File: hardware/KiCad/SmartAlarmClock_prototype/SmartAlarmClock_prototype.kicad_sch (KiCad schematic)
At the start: 18 parts, among them J1 YD-ESP32-S3 dev board, J2 MAX7219 32x8 module, J3 DS3231 RTC module (ZS-042), J4 Touch electrode, Q1 BSS138, Q2 BSS138, Q3 BSS138, Q4 BS170

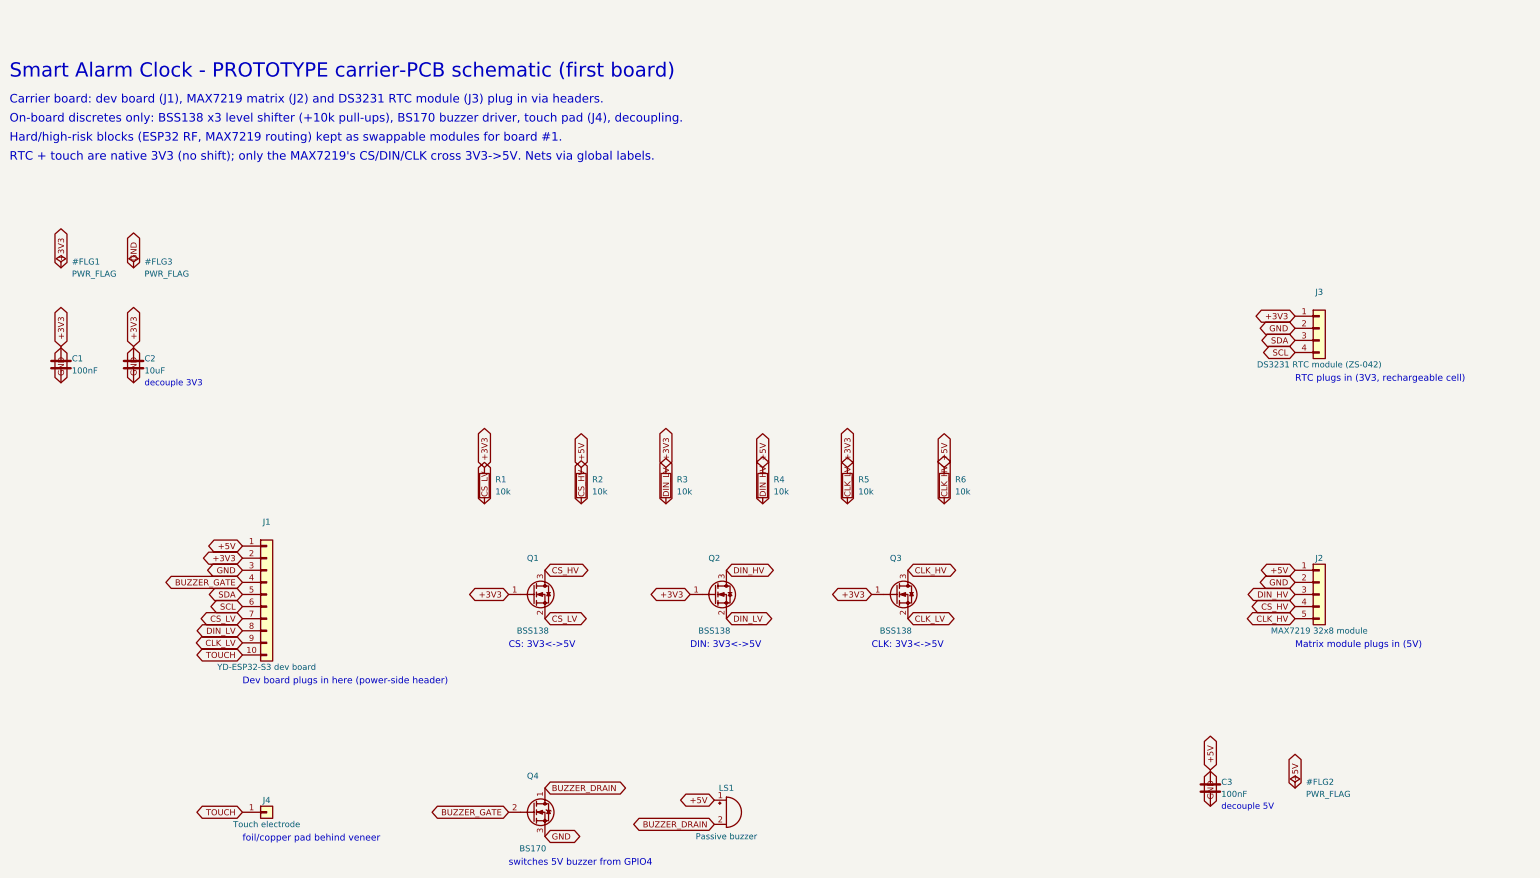
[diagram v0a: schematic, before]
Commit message: hardware: redraw prototype schematic as grouped functional blocks
Reorganize the prototype carrier schematic into labeled, boxed functional blocks
(Dev Board, Decoupling, Level Shifter, RTC/Matrix module headers, Buzzer, Touch)
like a real hand-drawn sheet. Power symbols for the rails, net labels for
cross-block signals, all wires strictly horizontal/vertical, labels placed to the
right of vertical wires / above horizontal ones, connector part-values hidden. ERC 0/0.

Co-Authored-By: Claude Opus 4.8 (1M context) <noreply@anthropic.com>
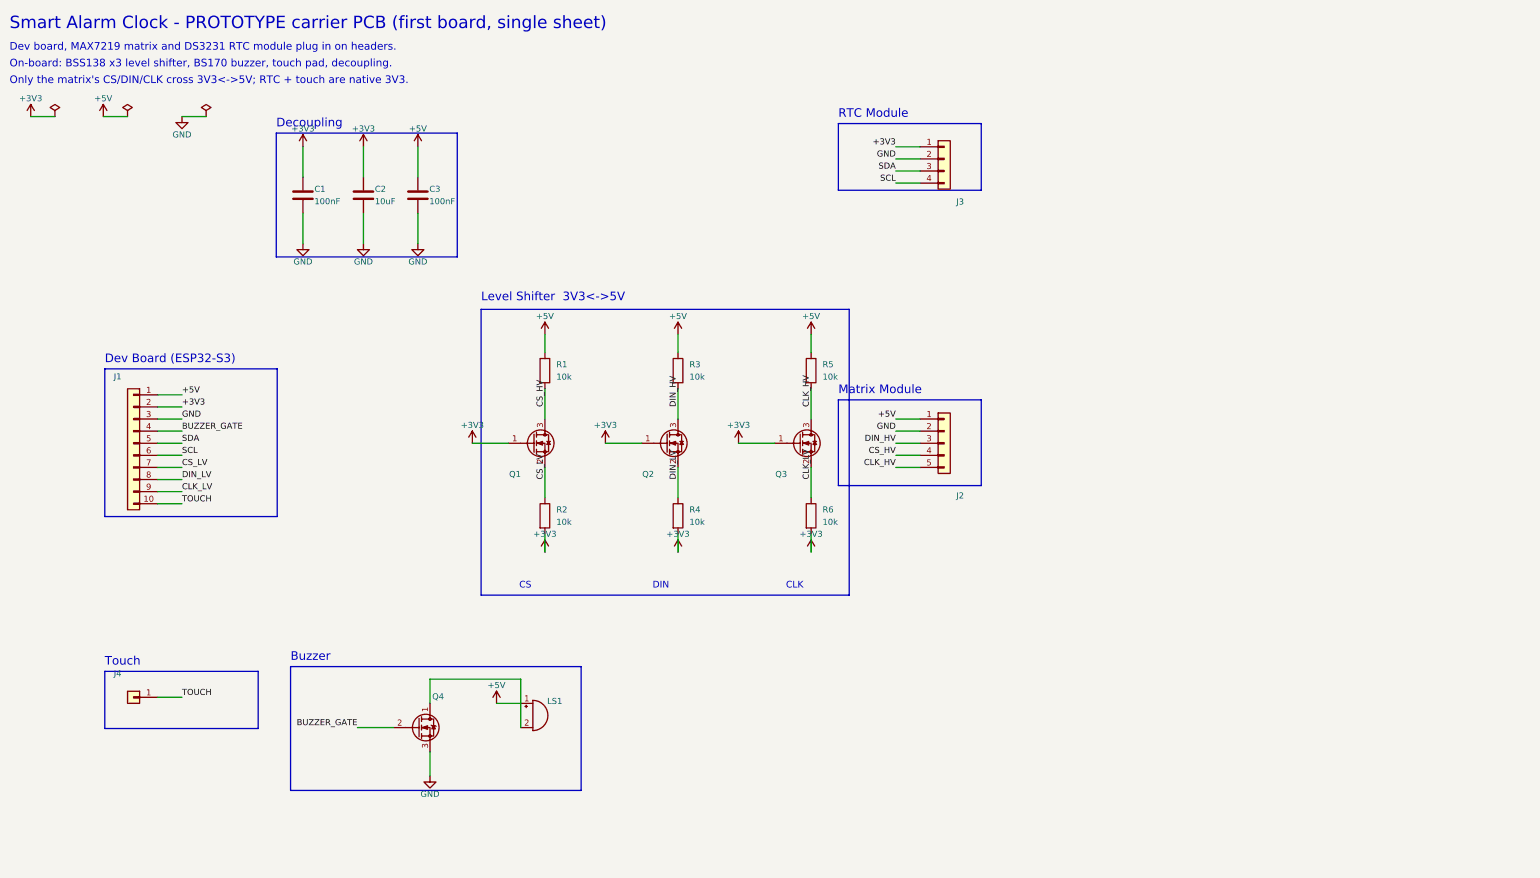
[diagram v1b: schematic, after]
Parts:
- removed C2: 10uF, symbol Device:C
- removed Q3: BSS138, symbol Transistor_FET:BSS138
- added J2: MAX7219, symbol Connector_Generic:Conn_01x05
- added R2: 10k, symbol Device:R
- C2: renamed from R2; value 10k -> 10uF; symbol Device:R -> Device:C
- J1: value YD-ESP32-S3 dev board -> YD-ESP32-S3
- J3: value DS3231 RTC module (ZS-042) -> DS3231
- J4: value Touch electrode -> Touch pad
- LS1: value Passive buzzer -> Buzzer
- Q3: renamed from J2; value MAX7219 32x8 module -> BSS138; symbol Connector_Generic:Conn_01x05 -> Transistor_FET:BSS138
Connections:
- net +3V3: now also C2.1, Q3.1 (G), R4.2, R6.2, R2.2; no longer R1.1, R3.1, R5.1
- net +5V: now also R1.1, R3.1, R5.1, J2.1 (Pin_1); no longer C2.1, Q3.1 (Pin_1), R4.1, R6.1
- net CLK_HV: now also Q3.3 (D), R5.2, J2.5 (Pin_5); no longer Q3.5 (Pin_5), R6.2
- net CLK_LV: now also Q3.2 (S), R6.1; no longer R5.2
- net CS_HV: now also R1.2, J2.4 (Pin_4); no longer C2.2, Q3.4 (Pin_4)
- net CS_LV: now also R2.1; no longer R1.2
- net DIN_HV: now also R3.2, J2.3 (Pin_3); no longer Q3.3 (Pin_3), R4.2
- net DIN_LV: now also R4.1; no longer R3.2
- net GND: now also C2.2, J2.2 (Pin_2); no longer Q3.2 (Pin_2)
- net BUZZER_DRAIN: no longer names the net of LS1.2 (-), Q4.1 (D)
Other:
- note added: "Buzzer"
- note added: "CLK"
- note added: "CS"
- note added: "DIN"
- note added: "Decoupling"
- note added: "Dev Board (ESP32-S3)"
- note added: "Dev board, MAX7219 matrix and DS3231 RTC module plug in on headers."
- note added: "Level Shifter 3V3<->5V"
- note added: "Matrix Module"
- note added: "On-board: BSS138 x3 level shifter, BS170 buzzer, touch pad, decoupling."
- note added: "Only the matrix's CS/DIN/CLK cross 3V3<->5V; RTC + touch are native 3V3."
- note added: "RTC Module"
- note added: "Smart Alarm Clock - PROTOTYPE carrier PCB (first board, single sheet)"
- note added: "Touch"
- note removed: "CLK: 3V3<->5V"
- note removed: "CS: 3V3<->5V"
- note removed: "Carrier board: dev board (J1), MAX7219 matrix (J2) and DS3231 RTC module (J3) plug in via headers."
- note removed: "DIN: 3V3<->5V"
- note removed: "Dev board plugs in here (power-side header)"
- note removed: "Hard/high-risk blocks (ESP32 RF, MAX7219 routing) kept as swappable modules for board #1."
- note removed: "Matrix module plugs in (5V)"
- note removed: "On-board discretes only: BSS138 x3 level shifter (+10k pull-ups), BS170 buzzer driver, touch pad (J4), decoupling."
- note removed: "RTC + touch are native 3V3 (no shift); only the MAX7219's CS/DIN/CLK cross 3V3->5V. Nets via global labels."
- note removed: "RTC plugs in (3V3, rechargeable cell)"
- note removed: "Smart Alarm Clock - PROTOTYPE carrier-PCB schematic (first board)"
- note removed: "decouple 3V3"
- note removed: "decouple 5V"
- note removed: "foil/copper pad behind veneer"
- note removed: "switches 5V buzzer from GPIO4"
